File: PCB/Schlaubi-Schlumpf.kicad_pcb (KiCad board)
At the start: 4 copper layers, 50 x 65 mm, 150 parts, among them IC1 ADS131E08IPAGR, IC2 TP4056, IC3 TLV9051IDBVR, IC5 TPS7A9101DSKR, IC7 LM2775QDSGRQ1, J1 8P8C_Shielded, J2 Conn_01x04_Socket, J3 Conn_01x04_Socket, J4 Conn_01x02_Pin, J5 8P8C_Shielded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

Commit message: Stemma etc.
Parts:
- R7: value 4k7 -> 3.57k
- moved FB2 4.21 mm to (112.0, 50.6)
- moved CS52 2.50 mm to (99.2, 90.3), turned to 180 degrees
- moved CS18 1.36 mm to (98.5, 74.0), turned to 180 degrees
- moved CS19 1.30 mm to (98.5, 72.5), turned to 180 degrees
- moved CS51 1.28 mm to (98.5, 99.6), turned to 0 degrees
- moved CS50 1.24 mm to (98.5, 101.1), turned to 0 degrees
- moved CS16 1.00 mm to (99.2, 83.2)
- moved CS17 1.00 mm to (99.2, 84.7)
- moved CS53 0.50 mm to (99.2, 88.8), turned to 180 degrees
- renumbered GPIO3 to GPIO1
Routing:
- net /ADC/Vbias: track 136.9 -> 145.3 mm, vias 6 -> 7
- net /Vbus: track 35.6 -> 28.4 mm
- net Net-(CS21-Pad2): track 3.72 -> 7.08 mm
- net GND: track 104.0 -> 102.1 mm, vias 106 -> 107
- net /ADC/AVDD: track 119.4 -> 120.1 mm
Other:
- board text added: "+ refers to Signal input - refers to Vbias"
- board text removed: "- refers to Vbias"

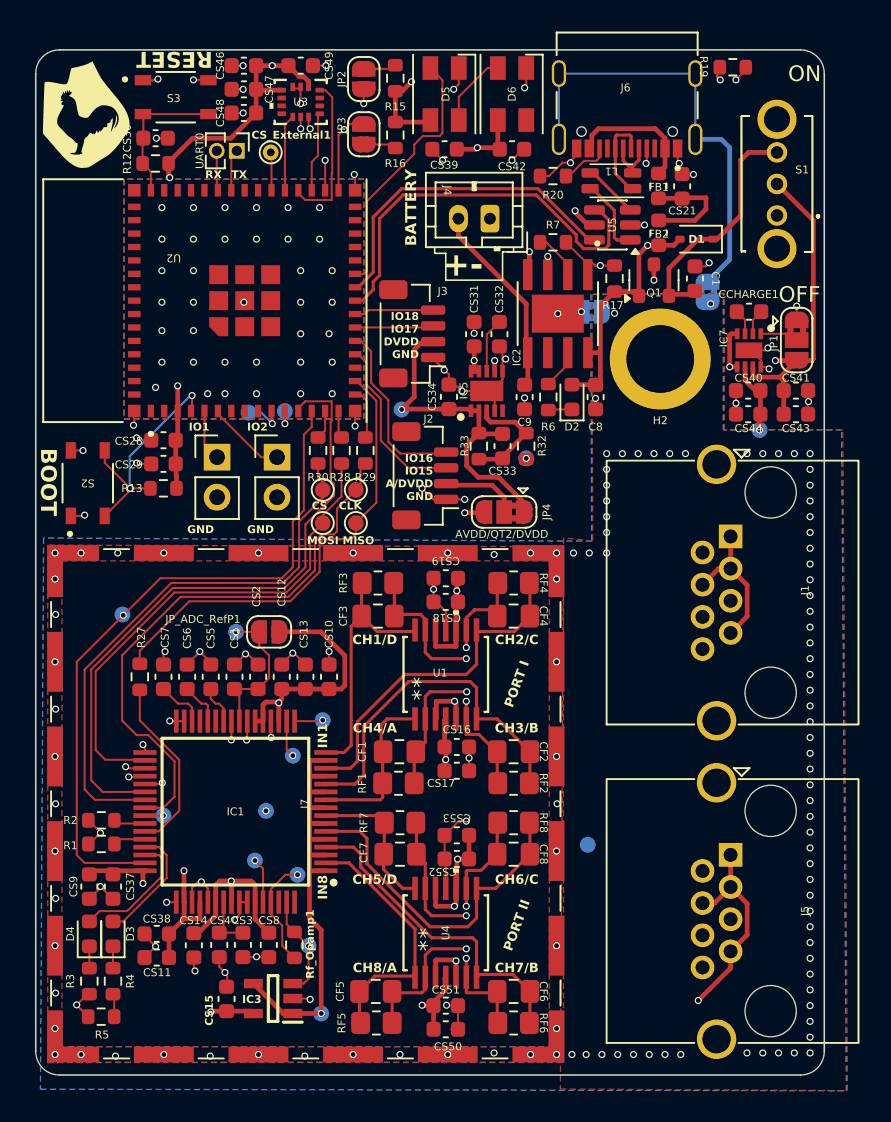
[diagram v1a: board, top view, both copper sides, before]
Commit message: Added Missing Components in Export
Issue was caused by the JLCPCB Plugin which does not export components with a name longer than 7 letters
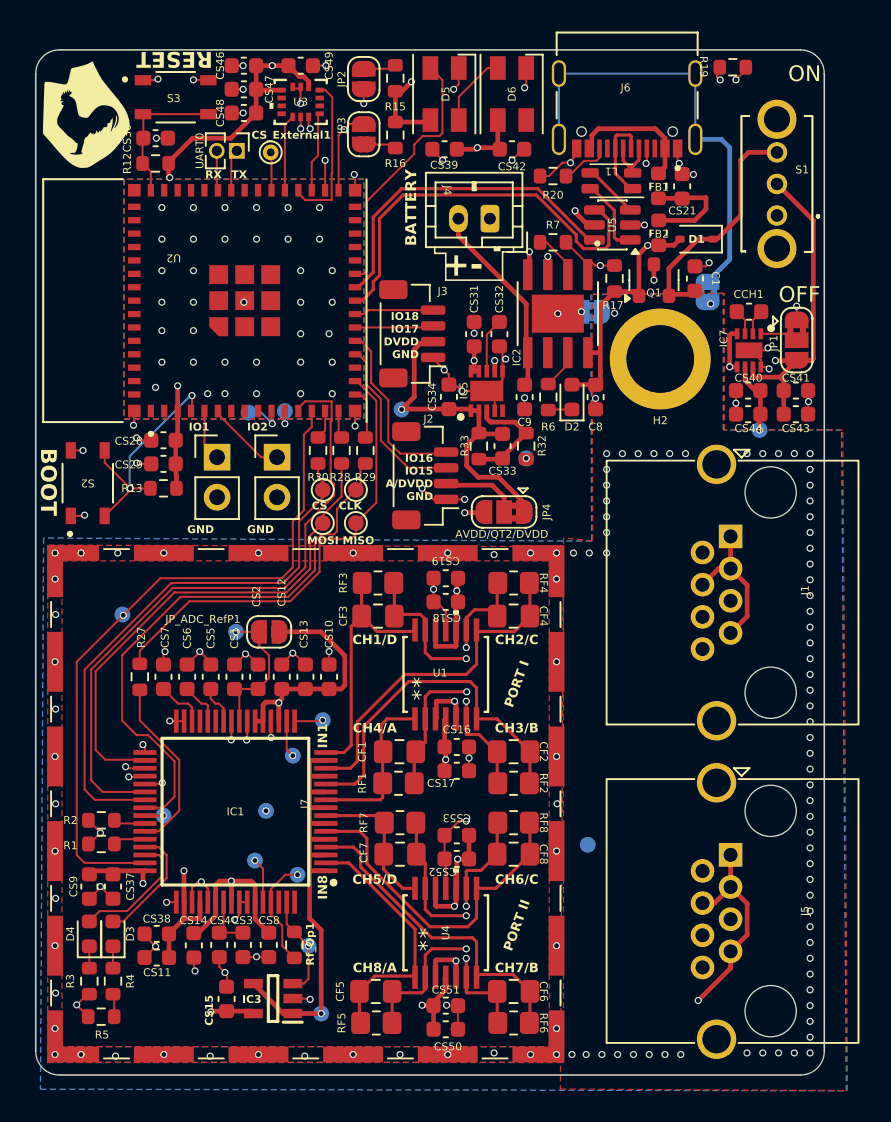
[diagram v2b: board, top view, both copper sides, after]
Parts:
- renumbered CCHARGE1 to CCH1, Rf_Opamp1 to Rf_Op1
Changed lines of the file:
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@@
 		(descr "Capacitor SMD 0603 (1608 Metric), square (rectangular) end terminal, IPC_7351 nominal, (Body size source: IPC-SM-782 page 76, https://www.pcb-3d.com/wordpress/wp-content/uploads/ipc-sm-782a_amendment_1_and_2.pdf), generated with kicad-footprint-generator")
 		(tags "capacitor")
-		(property "Reference" "CCHARGE1"
+		(property "Reference" "CCH1"
 			(at -0.025 -1.1 0)
 			(unlocked yes)
@@
 		(descr "Resistor SMD 0603 (1608 Metric), square (rectangular) end terminal, IPC_7351 nominal, (Body size source: IPC-SM-782 page 72, https://www.pcb-3d.com/wordpress/wp-content/uploads/ipc-sm-782a_amendment_1_and_2.pdf), generated with kicad-footprint-generator")
 		(tags "resistor")
-		(property "Reference" "Rf_Opamp1"
+		(property "Reference" "Rf_Op1"
 			(at -0.05 -1 90)
 			(unlocked yes)
